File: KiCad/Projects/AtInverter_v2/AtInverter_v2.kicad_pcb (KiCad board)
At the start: 2 copper layers, 83.8 x 94.6 mm, 116 parts, among them Q1 IRFB4020PBF, Q2 IRFB4020PBF, Q3 IRFB4020PBF, Q4 IRFB4020PBF, T1 ZMPT101B, U1 LM358N, U10 TLV61046ADB, U11 R-78HE5.0-0.3, U2 74LVC1G32, U3 LM393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

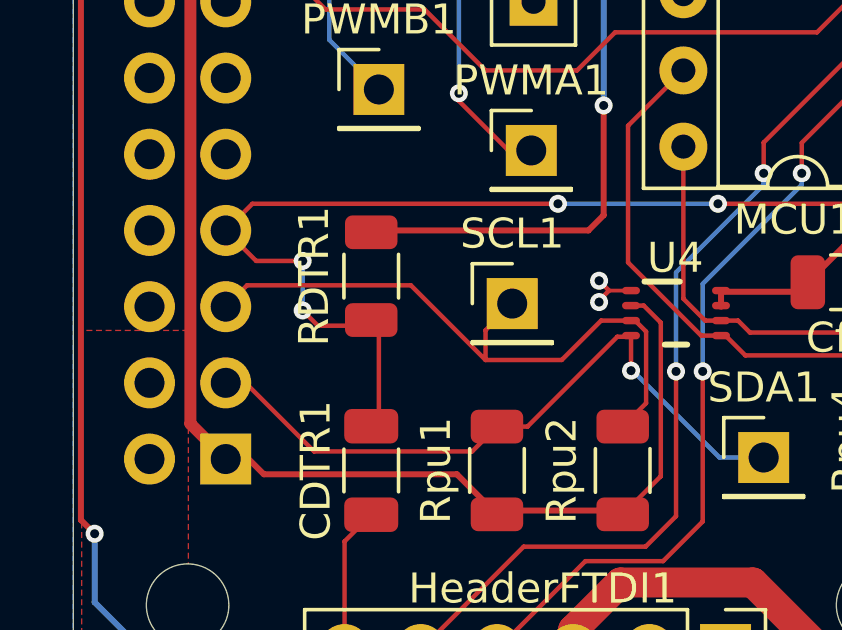
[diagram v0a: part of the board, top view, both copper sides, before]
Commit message: Added dedicated section for hardware description and high level diagrams
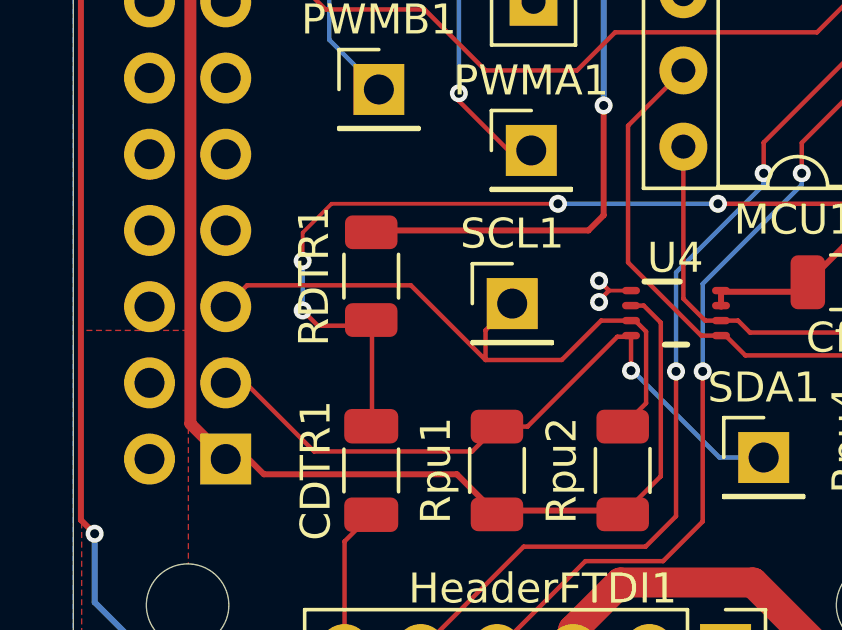
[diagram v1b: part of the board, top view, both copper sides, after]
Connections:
- PiConnector1 pad 7: /!RESET -> unconnected-(PiConnector1-GCLK0/GPIO4-Pad7)
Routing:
- net /!RESET: track 35.0 -> 30.2 mm
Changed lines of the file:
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@@
 	(net 105 "Net-(U10-FB)")
 	(net 106 "12V")
+	(net 107 "unconnected-(PiConnector1-GCLK0{slash}GPIO4-Pad7)")
 	(footprint "Connector_PinHeader_2.54mm:PinHeader_1x01_P2.54mm_Vertical"
 		(layer "F.Cu")
@@
 			(layers "*.Cu" "*.Mask")
 			(remove_unused_layers no)
-			(net 8 "/!RESET")
+			(net 107 "unconnected-(PiConnector1-GCLK0{slash}GPIO4-Pad7)")
 			(pinfunction "GCLK0/GPIO4")
-			(pintype "bidirectional")
+			(pintype "bidirectional+no_connect")
 		)
 		(pad "8" thru_hole oval
@@
 	)
 	(segment
-		(start 69.596 118.8212)
-		(end 68.58 117.8052)
-		(width 0.15)
+		(start 71.1454 117.8814)
+		(end 71.1454 118.8212)
+		(width 0.127)
 		(layer "F.Cu")
 		(net 8)
 	)
 	(segment
-		(start 73.6854 121.0457)
-		(end 73.4314 120.7917)
+		(start 73.4568 124.3058)
+		(end 73.4568 120.8171)
 		(width 0.15)
 		(layer "F.Cu")
@@
 	)
 	(segment
-		(start 79.6544 116.9162)
-		(end 69.469 116.9162)
+		(start 73.4568 120.8171)
+		(end 73.4314 120.7917)
 		(width 0.15)
 		(layer "F.Cu")
@@
 	)
 	(segment
-		(start 73.6854 124.0772)
-		(end 73.6854 121.0457)
-		(width 0.15)
+		(start 79.6544 116.9162)
+		(end 72.1106 116.9162)
+		(width 0.127)
 		(layer "F.Cu")
 		(net 8)
 	)
 	(segment
-		(start 69.469 116.9162)
-		(end 68.58 117.8052)
+		(start 71.1454 120.4722)
+		(end 71.6534 120.9802)
 		(width 0.15)
 		(layer "F.Cu")
@@
 	(segment
 		(start 73.4314 124.3312)
-		(end 73.6854 124.0772)
-		(width 0.15)
-		(layer "F.Cu")
-		(net 8)
-	)
-	(segment
-		(start 71.1454 120.4722)
-		(end 71.6534 120.9802)
+		(end 73.4568 124.3058)
 		(width 0.15)
 		(layer "F.Cu")
@@
 	)
 	(segment
-		(start 84.9884 116.9162)
-		(end 89.5504 116.9162)
-		(width 0.15)
+		(start 72.1106 116.9162)
+		(end 71.1454 117.8814)
+		(width 0.127)
 		(layer "F.Cu")
 		(net 8)
 	)
 	(segment
-		(start 71.1454 118.8212)
-		(end 69.596 118.8212)
+		(start 84.9884 116.9162)
+		(end 89.5504 116.9162)
 		(width 0.15)
 		(layer "F.Cu")

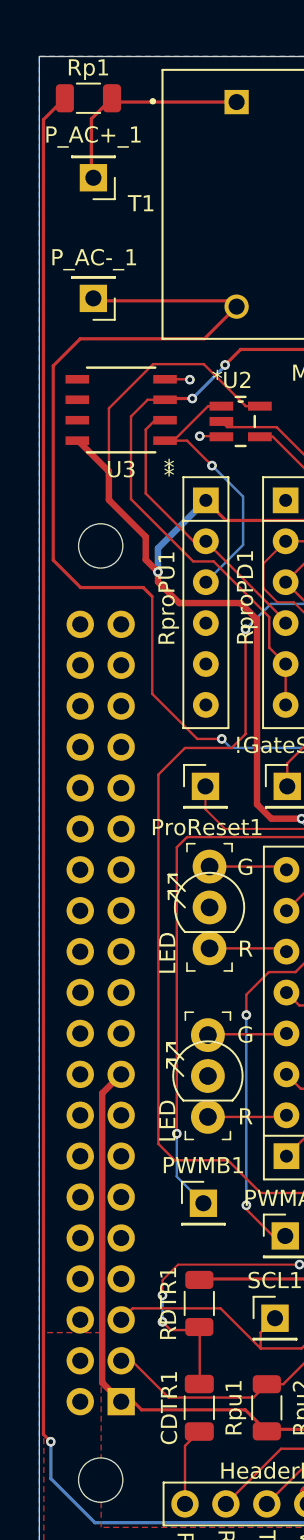
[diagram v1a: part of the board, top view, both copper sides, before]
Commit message: modifications to a_v2 hardware docs section
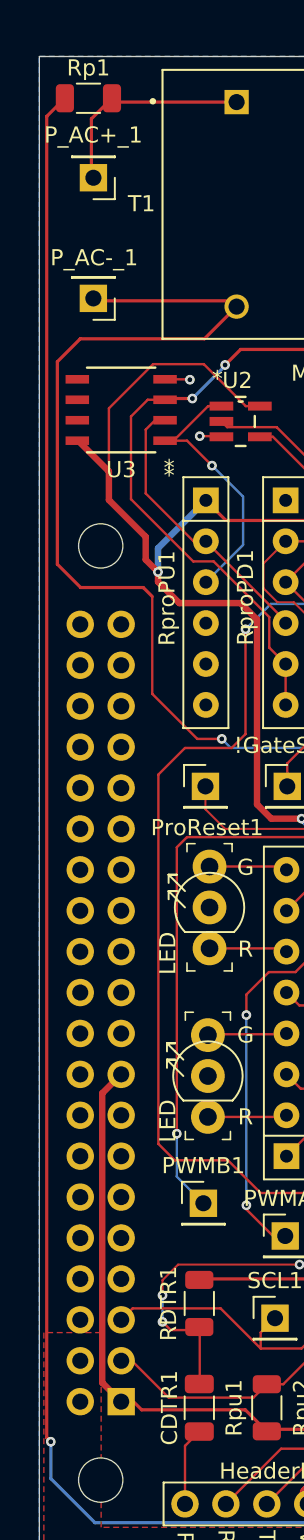
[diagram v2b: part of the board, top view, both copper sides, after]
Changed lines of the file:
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@@
 	)
 	(segment
-		(start 66.04 59.436)
-		(end 73.749 59.436)
+		(start 66.8528 56.9266)
+		(end 67.0052 57.079)
 		(width 0.2)
 		(layer "F.Cu")
@@
 	)
 	(segment
-		(start 66.8528 56.9266)
-		(end 67.0052 57.079)
+		(start 75.3872 57.079)
+		(end 75.7466 57.4384)
 		(width 0.2)
 		(layer "F.Cu")
@@
 	)
 	(segment
-		(start 75.3872 57.079)
-		(end 75.7466 57.4384)
+		(start 64.6176 60.8584)
+		(end 66.04 59.436)
 		(width 0.2)
 		(layer "F.Cu")
@@
 	)
 	(segment
-		(start 73.749 59.436)
-		(end 75.7466 57.4384)
+		(start 69.9516 74.8792)
+		(end 66.0654 74.8792)
 		(width 0.2)
 		(layer "F.Cu")
@@
 	)
 	(segment
-		(start 66.0654 74.8792)
-		(end 64.3636 73.1774)
+		(start 64.6176 73.4314)
+		(end 64.6176 60.8584)
 		(width 0.2)
 		(layer "F.Cu")
@@
 	)
 	(segment
-		(start 64.3636 73.1774)
-		(end 64.3636 61.1124)
+		(start 66.0654 74.8792)
+		(end 64.6176 73.4314)
 		(width 0.2)
 		(layer "F.Cu")
@@
 	)
 	(segment
-		(start 64.3636 61.1124)
-		(end 66.04 59.436)
-		(width 0.2)
-		(layer "F.Cu")
-		(net 1)
-	)
-	(segment
-		(start 70.5104 75.438)
-		(end 69.9516 74.8792)
+		(start 73.749 59.436)
+		(end 75.7466 57.4384)
 		(width 0.2)
 		(layer "F.Cu")
@@
 	)
 	(segment
-		(start 69.9516 74.8792)
-		(end 66.0654 74.8792)
+		(start 70.5104 75.438)
+		(end 69.9516 74.8792)
+		(width 0.2)
+		(layer "F.Cu")
+		(net 1)
+	)
+	(segment
+		(start 66.04 59.436)
+		(end 73.749 59.436)
 		(width 0.2)
 		(layer "F.Cu")
@@
 	(segment
 		(start 64.2112 127.9144)
-		(end 63.754 127.4572)
+		(end 63.9572 127.6604)
 		(width 0.2)
 		(layer "F.Cu")
@@
 	)
 	(segment
-		(start 63.754 45.8323)
-		(end 65.0855 44.5008)
+		(start 126.532 132.9944)
+		(end 131.2564 128.27)
 		(width 0.2)
 		(layer "F.Cu")
@@
 	)
 	(segment
-		(start 126.532 132.9944)
-		(end 131.2564 128.27)
+		(start 93.5228 132.9108)
+		(end 93.6064 132.9944)
 		(width 0.2)
 		(layer "F.Cu")
@@
 	)
 	(segment
-		(start 93.5228 132.9108)
-		(end 93.6064 132.9944)
+		(start 93.6064 132.9944)
+		(end 126.532 132.9944)
 		(width 0.2)
 		(layer "F.Cu")
@@
 	)
 	(segment
-		(start 63.754 127.4572)
-		(end 63.754 45.8323)
+		(start 63.9572 45.6291)
+		(end 65.0855 44.5008)
 		(width 0.2)
 		(layer "F.Cu")
@@
 	)
 	(segment
-		(start 93.6064 132.9944)
-		(end 126.532 132.9944)
+		(start 63.9572 127.6604)
+		(end 63.9572 45.6291)
 		(width 0.2)
 		(layer "F.Cu")
